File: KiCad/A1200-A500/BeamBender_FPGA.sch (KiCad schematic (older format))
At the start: 29 parts, among them J6 Conn_02x06_Odd_Even, U2 GW1NR-UV9LQ144P, U5 AK5720VT, X2 5.0x3.2mm

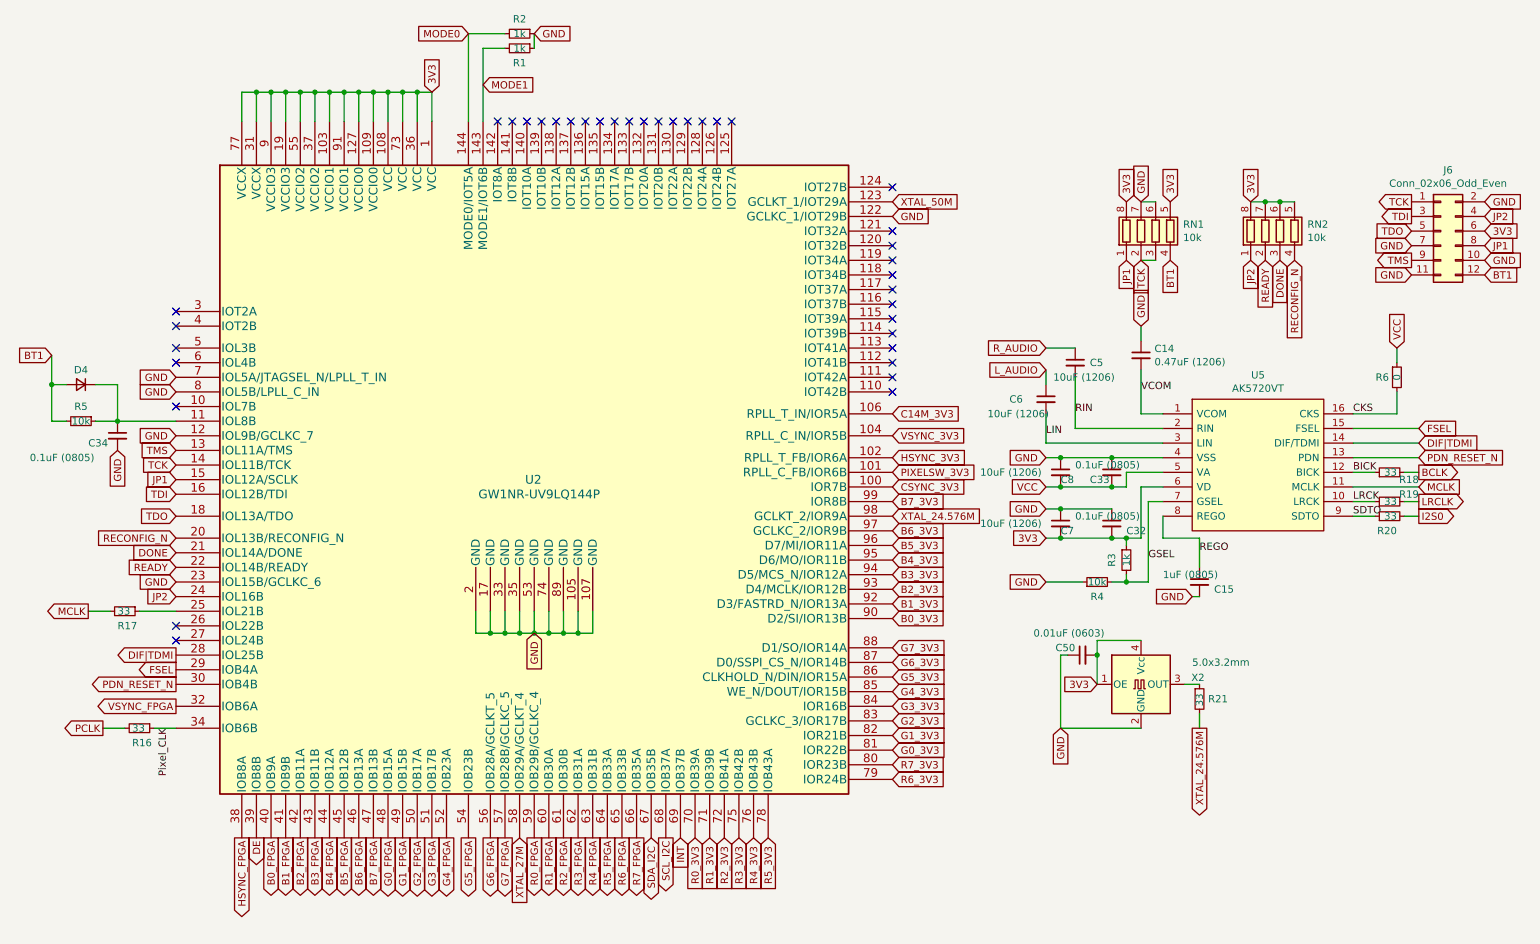
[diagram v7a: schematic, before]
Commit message: Adapted design to take 1.8V on VCCIO3 because of embedded pSRAM requirement, changed RN1, RN2 to 4.7k Ohm, relocated pin FSEL and DIF/TDMI to bank0, moved PDN_RESET_N to pin 29 and MCLK to pin 30. JP2 to pin 28, pin 7,8,12,23 changed to NC from GND, added pull-up for JTAG_TDO signal.
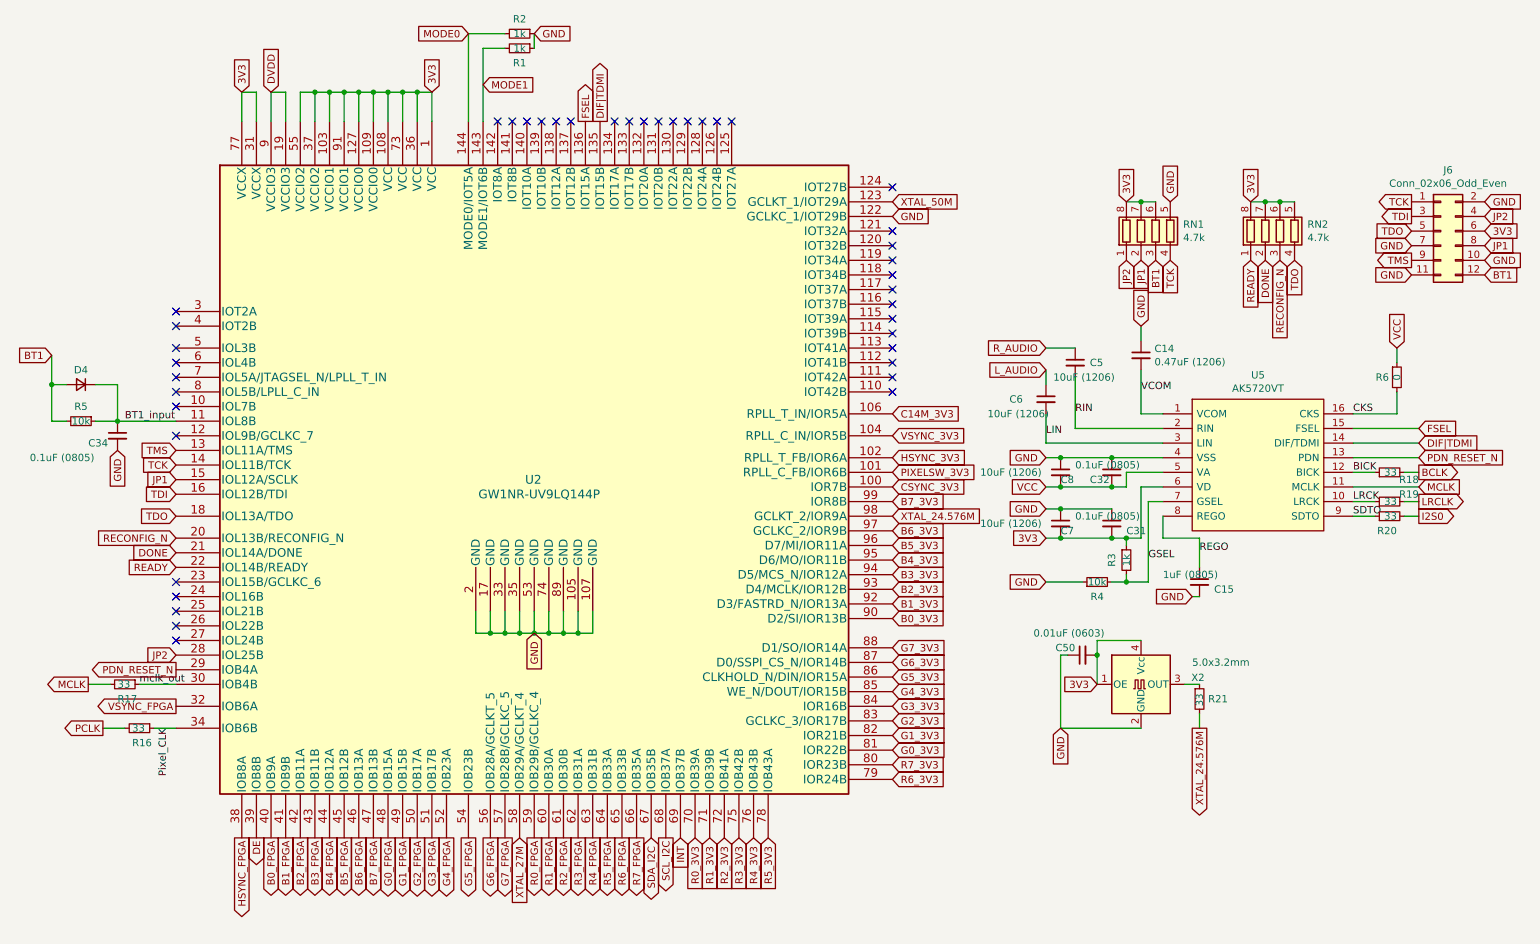
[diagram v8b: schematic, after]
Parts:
- RN1, RN2: value 10k -> 4.7k
- renumbered C32 to C31, C33 to C32
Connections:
- net 3V3: now also RN1.6 (R3.2), RN1.7 (R2.2); no longer RN1.5 (R4.2), U2.19 (VCCIO3), U2.9 (VCCIO3)
- net BT1: now also RN1.3 (R3.1); no longer RN1.4 (R4.1)
- net DIF|TDMI: now also U2.135 (IOT15B); no longer U2.28 (IOL25B)
- net DONE: now also RN2.2 (R2.1); no longer RN2.3 (R3.1)
- net FSEL: now also U2.136 (IOT15A); no longer U2.29 (IOB4A)
- net GND: now also RN1.5 (R4.2); no longer RN1.6 (R3.2), RN1.7 (R2.2), U2.12 (IOL9B/GCLKC_7), U2.23 (IOL15B/GCLKC_6), U2.7 (IOL5A/JTAGSEL_N/LPLL_T_IN), U2.8 (IOL5B/LPLL_C_IN)
- net JP1: now also RN1.2 (R2.1); no longer RN1.1 (R1.1)
- net JP2: now also RN1.1 (R1.1), U2.28 (IOL25B); no longer RN2.1 (R1.1), U2.24 (IOL16B)
- net PDN_RESET_N: now also U2.29 (IOB4A); no longer U2.30 (IOB4B)
- net READY: now also RN2.1 (R1.1); no longer RN2.2 (R2.1)
- net RECONFIG_N: now also RN2.3 (R3.1); no longer RN2.4 (R4.1)
- net TCK: now also RN1.4 (R4.1); no longer RN1.2 (R2.1), RN1.3 (R3.1)
- net TDO: now also RN2.4 (R4.1)
- net BT1_input: now reaches C34.1, D4.1 (K), R5.1, U2.11 (IOL8B)
- net at U2.25 (IOL21B): no longer R17.1
- new net DVDD: U2.19 (VCCIO3), U2.9 (VCCIO3)
- new net mclk_out: R17.1, U2.30 (IOB4B)
- no-connect marks 37 -> 41
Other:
- moved on the sheet: R17
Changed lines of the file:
@@
 Wire Wire Line
 	2150 1250 2150 1050
-Connection ~ 2150 1050
-Wire Wire Line
-	2150 1050 2250 1050
 Wire Wire Line
 	2250 1250 2250 1050
-Connection ~ 2250 1050
-Wire Wire Line
-	2250 1050 2350 1050
 Wire Wire Line
 	2350 1250 2350 1050
-Connection ~ 2350 1050
-Wire Wire Line
-	2350 1050 2450 1050
 Wire Wire Line
 	2450 1250 2450 1050
-Connection ~ 2450 1050
 Wire Wire Line
 	2450 1050 2550 1050
@@
 Text GLabel 3700 1000 2    50   Input ~ 0
 MODE1
-Text GLabel 1600 3100 0    50   Input ~ 0
-GND
-Text GLabel 1600 3400 0    50   Input ~ 0
-GND
 Text GLabel 1600 3700 0    50   Input ~ 0
 JP1
-Text GLabel 1600 4400 0    50   Input ~ 0
-GND
-Text GLabel 1600 3000 0    50   Input ~ 0
-GND
 NoConn ~ 1600 2550
 NoConn ~ 1600 2650
@@
 NoConn ~ 4200 1250
 NoConn ~ 4300 1250
-NoConn ~ 4400 1250
-NoConn ~ 4500 1250
 NoConn ~ 4600 1250
 NoConn ~ 4700 1250
@@
 P 8300 2000
 F 0 "RN1" H 8488 2046 50  0000 L CNN
-F 1 "10k" H 8488 1955 50  0000 L CNN
+F 1 "4.7k" H 8488 1955 50  0000 L CNN
 F 2 "BeamBender:RESCAF80P320X160X60-8N" V 8575 2000 50  0001 C CNN
 F 3 "~" H 8300 2000 50  0001 C CNN
@@
 	1    0    0    -1
 $EndComp
+Wire Wire Line
+	4050 650  4050 750
+Text GLabel 8200 2200 3    50   Input ~ 0
+JP1
+Text GLabel 8400 2200 3    50   Input ~ 0
+TCK
 Text GLabel 8400 1800 1    50   Input ~ 0
-3V3
-Wire Wire Line
-	4050 650  4050 750
+GND
 Text GLabel 8100 2200 3    50   Input ~ 0
-JP1
-Text GLabel 8200 2200 3    50   Input ~ 0
-TCK
-Text GLabel 8200 1800 1    50   Input ~ 0
-GND
+JP2
+Text GLabel 9150 2200 3    50   Input ~ 0
+RECONFIG_N
+Text GLabel 9050 2200 3    50   Input ~ 0
+DONE
 Text GLabel 8950 2200 3    50   Input ~ 0
-JP2
-Text GLabel 9250 2200 3    50   Input ~ 0
-RECONFIG_N
-Text GLabel 9150 2200 3    50   Input ~ 0
-DONE
-Text GLabel 9050 2200 3    50   Input ~ 0
 READY
 $Comp
@@
 P 9150 2000
 F 0 "RN2" H 9338 2046 50  0000 L CNN
-F 1 "10k" H 9338 1955 50  0000 L CNN
+F 1 "4.7k" H 9338 1955 50  0000 L CNN
 F 2 "BeamBender:RESCAF80P320X160X60-8N" V 9425 2000 50  0001 C CNN
 F 3 "~" H 9150 2000 50  0001 C CNN
@@
 Wire Wire Line
 	9150 1800 9250 1800
-Text GLabel 8400 2200 3    50   Input ~ 0
+Text GLabel 8300 2200 3    50   Input ~ 0
 BT1
 Text GLabel 10050 1800 0    50   Output ~ 0
@@
 Text GLabel 10550 2000 2    50   Input ~ 0
 3V3
-Text GLabel 1600 4500 0    50   Input ~ 0
+Text GLabel 1600 4900 0    50   Input ~ 0
 JP2
 Text GLabel 750  2850 0    50   Input ~ 0
@@
 Text GLabel 10550 1900 2    50   Input ~ 0
 JP2
-Wire Wire Line
-	8200 1800 8300 1800
-Wire Wire Line
-	8200 2200 8300 2200
 Text GLabel 8100 1800 1    50   Input ~ 0
 3V3
@@
 Text GLabel 6500 3950 2    50   Input ~ 0
 XTAL_24.576M
-Text GLabel 1000 4600 0    50   Output ~ 0
+Text GLabel 1000 5100 0    50   Output ~ 0
 MCLK
 $Comp
 L Device:R_Small R?
 U 1 1 666738D2
-P 1250 4600
+P 1250 5100
 AR Path="/666738D2" Ref="R?"  Part="1"
 AR Path="/6541C824/666738D2" Ref="R17"  Part="1"
-F 0 "R17" V 1350 4550 50  0000 L CNN
-F 1 "33" V 1250 4550 50  0000 L CNN
-F 2 "Resistor_SMD:R_0603_1608Metric_Pad0.98x0.95mm_HandSolder" H 1250 4600 50  0001 C CNN
-F 3 "~" H 1250 4600 50  0001 C CNN
-	1    1250 4600
+F 0 "R17" V 1350 5050 50  0000 L CNN
+F 1 "33" V 1250 5050 50  0000 L CNN
+F 2 "Resistor_SMD:R_0603_1608Metric_Pad0.98x0.95mm_HandSolder" H 1250 5100 50  0001 C CNN
+F 3 "~" H 1250 5100 50  0001 C CNN
+	1    1250 5100
 	0    1    1    0
 $EndComp
 Wire Wire Line
-	1150 4600 1000 4600
-Wire Wire Line
-	1350 4600 1600 4600
+	1150 5100 1000 5100
+Wire Wire Line
+	1350 5100 1600 5100
 $Comp
 L Device:R_Small R18
@@
 P 8000 3650
 AR Path="/66811715" Ref="C?"  Part="1"
-AR Path="/6541C824/66811715" Ref="C33"  Part="1"
-F 0 "C33" H 7850 3600 50  0000 L CNN
+AR Path="/6541C824/66811715" Ref="C32"  Part="1"
+F 0 "C32" H 7850 3600 50  0000 L CNN
 F 1 "0.1uF (0805)" H 7750 3700 50  0000 L CNN
 F 2 "Capacitor_SMD:C_0805_2012Metric_Pad1.18x1.45mm_HandSolder" H 8000 3650 50  0001 C CNN
@@
 P 8000 4000
 AR Path="/66848700" Ref="C?"  Part="1"
-AR Path="/6541C824/66848700" Ref="C32"  Part="1"
-F 0 "C32" H 8100 3950 50  0000 L CNN
+AR Path="/6541C824/66848700" Ref="C31"  Part="1"
+F 0 "C31" H 8100 3950 50  0000 L CNN
 F 1 "0.1uF (0805)" H 7750 4050 50  0000 L CNN
 F 2 "Capacitor_SMD:C_0805_2012Metric_Pad1.18x1.45mm_HandSolder" H 8000 4000 50  0001 C CNN
@@
 Wire Wire Line
 	9650 3750 10100 3750
-Text GLabel 1600 5100 0    50   Output ~ 0
+Text GLabel 1600 5000 0    50   Output ~ 0
 PDN_RESET_N
-Text GLabel 1600 4900 0    50   Output ~ 0
+Text GLabel 4500 1250 1    50   Output ~ 0
 DIF|TDMI
 Text GLabel 10100 3350 2    50   Input ~ 0
@@
 Wire Wire Line
 	9650 3350 10100 3350
-Text GLabel 1600 5000 0    50   Output ~ 0
+Text GLabel 4400 1250 1    50   Output ~ 0
 FSEL
 $Comp
@@
 Wire Wire Line
 	7550 4400 7800 4400
+Wire Wire Line
+	2250 1050 2350 1050
+Text GLabel 2050 1050 1    50   Input ~ 0
+3V3
+Text GLabel 2250 1050 1    50   Input ~ 0
+DVDD
+NoConn ~ 1600 3000
+NoConn ~ 1600 3100
+NoConn ~ 1600 3400
+NoConn ~ 1600 4400
+Text Label 1350 5100 0    50   ~ 0
+mclk_out
+NoConn ~ 1600 4600
+Text GLabel 9250 2200 3    50   Input ~ 0
+TDO
+NoConn ~ 1600 4500
+Text Label 1250 3300 0    50   ~ 0
+BT1_input
+Wire Wire Line
+	8100 1800 8200 1800
+Connection ~ 8200 1800
+Wire Wire Line
+	8200 1800 8300 1800
 $EndSCHEMATC
